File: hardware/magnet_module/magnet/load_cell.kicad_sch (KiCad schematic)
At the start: 12 parts, among them J7 Conn_01x04_Pin, U4 NAU7802, U5 KC2520Z4.91520C1KX00

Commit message: sensor design
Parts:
- J7: value Conn_01x04_Pin -> 691137710004
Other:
- note added: "Load Cell Input"
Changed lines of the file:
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@@
+		)
+	)
+	(text "Load Cell Input"
+		(exclude_from_sim no)
+		(at 53.086 72.136 0)
+		(effects
+			(font
+				(size 1.27 1.27)
+			)
 		)
 	)
@@
 	(label "CELL.SCL"
 		(at 156.21 85.09 0)
+		(fields_autoplaced yes)
 		(effects
 			(font
@@
 	(label "CELL.SDA"
 		(at 156.21 87.63 0)
+		(fields_autoplaced yes)
 		(effects
 			(font
@@
 			)
 		)
-		(property "Value" "Conn_01x04_Pin"
+		(property "Value" "691137710004"
 			(at 64.262 64.77 0)
 			(effects
@@
 			(at 63.5 71.12 0)
 			(effects
+				(font
+					(size 1.27 1.27)
+				)
+				(hide yes)
+			)
+		)
+		(property "MPN" ""
+			(at 63.5 71.12 0)
+			(effects

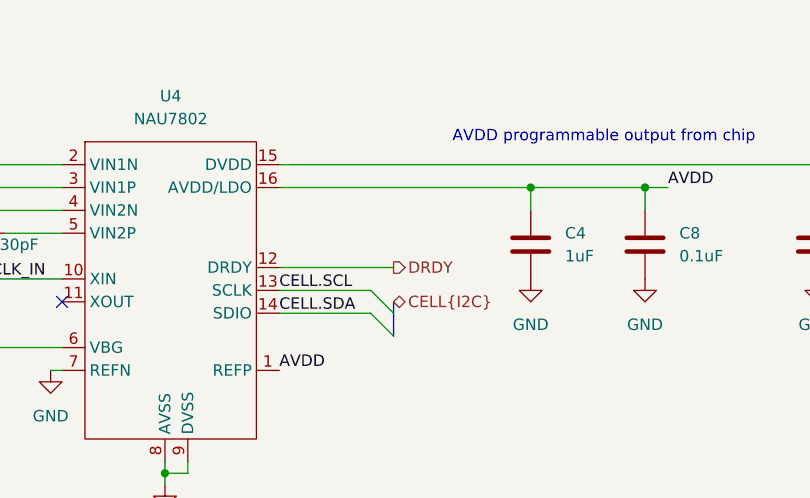
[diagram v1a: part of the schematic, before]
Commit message: fix erc errors
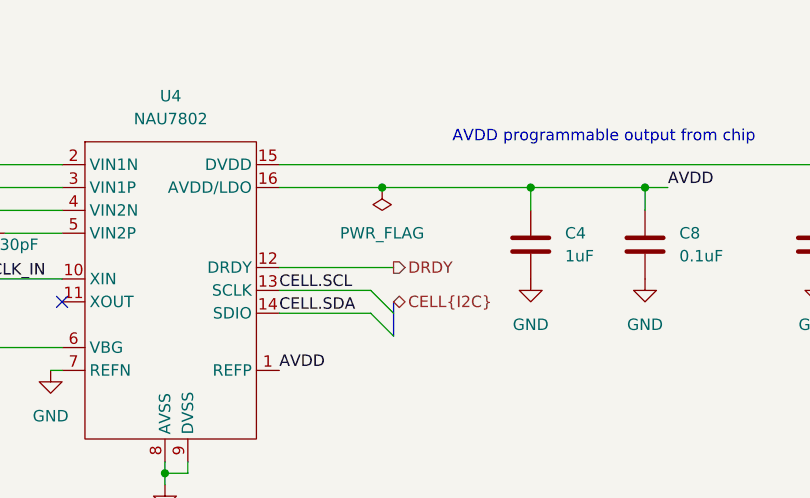
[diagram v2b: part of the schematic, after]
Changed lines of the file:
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@@
+	)
+	(junction
+		(at 167.64 73.66)
+		(diameter 0)
+		(color 0 0 0 0)
 	)
 	(junction
@@
 	(wire
 		(pts
-			(xy 184.15 73.66) (xy 156.21 73.66)
+			(xy 184.15 73.66) (xy 167.64 73.66)
 		)
 		(stroke
@@
 		(pts
 			(xy 118.11 78.74) (xy 114.3 78.74)
+		)
+		(stroke
+			(width 0)
+			(type default)
+		)
+	)
+	(wire
+		(pts
+			(xy 167.64 73.66) (xy 156.21 73.66)
 		)
 		(stroke
@@
 					(unit 1)
 				)
+			)
+		)
+	)
+	(symbol
+		(lib_id "power:PWR_FLAG")
+		(at 167.64 73.66 180)
+		(unit 1)
+		(exclude_from_sim no)
+		(in_bom yes)
+		(on_board yes)
+		(dnp no)
+		(fields_autoplaced yes)
+		(property "Reference" "#FLG01"
+			(at 167.64 75.565 0)
+			(effects
+				(font
+					(size 1.27 1.27)
+				)
+				(hide yes)
+			)
+		)
+		(property "Value" "PWR_FLAG"
+			(at 167.64 78.74 0)
+			(effects
+				(font
+					(size 1.27 1.27)
+				)
+			)
+		)
+		(property "Footprint" ""
+			(at 167.64 73.66 0)
+			(effects
+				(font
+					(size 1.27 1.27)
+				)
+				(hide yes)
+			)
+		)
+		(property "Datasheet" "~"
+			(at 167.64 73.66 0)
+			(effects
+				(font
+					(size 1.27 1.27)
+				)
+				(hide yes)
+			)
+		)
+		(property "Description" "Special symbol for telling ERC where power comes from"
+			(at 167.64 73.66 0)
+			(effects
+				(font
+					(size 1.27 1.27)
+				)
+				(hide yes)
+			)
+		)
+		(pin "1"
+		)
+		(instances
+			(project ""
+				(path "/aa5044b8-67cd-4b5a-a593-0df9431eb095/7846e2cb-93ba-4d8e-9136-73b0c490a979"
+					(reference "#FLG01")
+					(unit 1)
+				)
